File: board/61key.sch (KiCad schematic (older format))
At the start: 134 parts, among them J1 105450-0101, SW1 SW_SPST, SW10 SW_SPST, SW11 SW_SPST, SW12 SW_SPST, SW13 SW_SPST, SW14 SW_SPST, SW15 SW_SPST, SW16 SW_SPST, SW17 SW_SPST, SW18 SW_SPST, SW19 SW_SPST, SW2 SW_SPST, SW20 SW_SPST, SW21 SW_SPST, SW22 SW_SPST, SW23 SW_SPST, SW24 SW_SPST, SW25 SW_SPST, SW26 SW_SPST, SW27 SW_SPST, SW28 SW_SPST, SW29 SW_SPST, SW3 SW_SPST, SW30 SW_SPST, SW31 SW_SPST, SW32 SW_SPST, SW33 SW_SPST, SW34 SW_SPST, SW35 SW_SPST, SW36 SW_SPST, SW37 SW_SPST, SW38 SW_SPST, SW39 SW_SPST, SW4 SW_SPST, SW40 SW_SPST, SW41 SW_SPST, SW42 SW_SPST, SW43 SW_SPST, SW44 SW_SPST, SW45 SW_SPST, SW46 SW_SPST, SW47 SW_SPST, SW48 SW_SPST, SW49 SW_SPST, SW5 SW_SPST, SW50 SW_SPST, SW51 SW_SPST, SW52 SW_SPST, SW53 SW_SPST, SW54 SW_SPST, SW55 SW_SPST, SW56 SW_SPST, SW57 SW_SPST, SW58 SW_SPST, SW59 SW_SPST, SW6 SW_SPST, SW60 SW_SPST, SW61 SW_SPST, SW7 SW_SPST, SW8 SW_SPST, SW9 SW_SPST, U1 ATmega32U4-AU, X1 FA-238

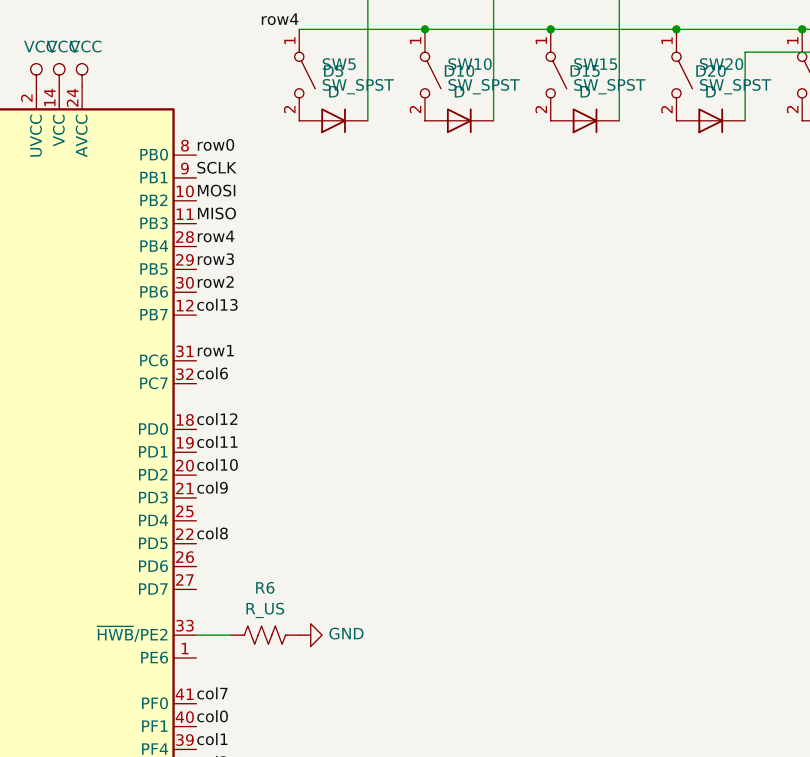
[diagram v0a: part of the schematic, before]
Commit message: add pads, new step
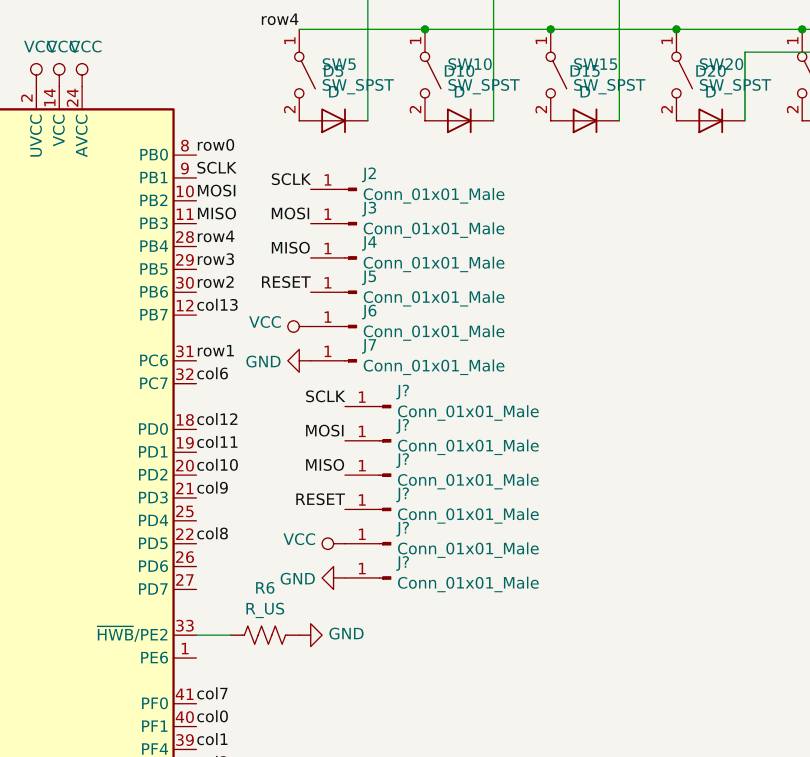
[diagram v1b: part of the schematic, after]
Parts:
- added J2, J3, J4, J5, J6, J7, J? (x6): Conn_01x01_Male, TestPoint:TestPoint_Pad_3.0x3.0mm, symbol Connector:Conn_01x01_Male
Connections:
- net GND: now also J7.1 (Pin_1), J?.1 (Pin_1)
- net MISO: now also J4.1 (Pin_1), J?.1 (Pin_1)
- net MOSI: now also J3.1 (Pin_1), J?.1 (Pin_1)
- net RESET: now also J5.1 (Pin_1), J?.1 (Pin_1)
- net SCLK: now also J2.1 (Pin_1), J?.1 (Pin_1)
- net VCC: now also J6.1 (Pin_1), J?.1 (Pin_1)
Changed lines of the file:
@@
 Text Label 5500 6850 0    50   ~ 0
 col1
+$Comp
+L Connector:Conn_01x01_Male J2
+U 1 1 5EB6BFE2
+P 6200 4400
+F 0 "J2" H 6172 4332 50  0000 R CNN
+F 1 "Conn_01x01_Male" H 6172 4423 50  0000 R CNN
+F 2 "TestPoint:TestPoint_Pad_3.0x3.0mm" H 6200 4400 50  0001 C CNN
+F 3 "~" H 6200 4400 50  0001 C CNN
+	1    6200 4400
+	-1   0    0    1
+$EndComp
+$Comp
+L Connector:Conn_01x01_Male J3
+U 1 1 5EB6DDE5
+P 6200 4550
+F 0 "J3" H 6172 4482 50  0000 R CNN
+F 1 "Conn_01x01_Male" H 6172 4573 50  0000 R CNN
+F 2 "TestPoint:TestPoint_Pad_3.0x3.0mm" H 6200 4550 50  0001 C CNN
+F 3 "~" H 6200 4550 50  0001 C CNN
+	1    6200 4550
+	-1   0    0    1
+$EndComp
+$Comp
+L Connector:Conn_01x01_Male J4
+U 1 1 5EB748FF
+P 6200 4700
+F 0 "J4" H 6172 4632 50  0000 R CNN
+F 1 "Conn_01x01_Male" H 6172 4723 50  0000 R CNN
+F 2 "TestPoint:TestPoint_Pad_3.0x3.0mm" H 6200 4700 50  0001 C CNN
+F 3 "~" H 6200 4700 50  0001 C CNN
+	1    6200 4700
+	-1   0    0    1
+$EndComp
+$Comp
+L Connector:Conn_01x01_Male J5
+U 1 1 5EB7B587
+P 6200 4850
+F 0 "J5" H 6172 4782 50  0000 R CNN
+F 1 "Conn_01x01_Male" H 6172 4873 50  0000 R CNN
+F 2 "TestPoint:TestPoint_Pad_3.0x3.0mm" H 6200 4850 50  0001 C CNN
+F 3 "~" H 6200 4850 50  0001 C CNN
+	1    6200 4850
+	-1   0    0    1
+$EndComp
+Text Label 6000 4400 2    50   ~ 0
+SCLK
+Text Label 6000 4550 2    50   ~ 0
+MOSI
+Text Label 6000 4700 2    50   ~ 0
+MISO
+Text Label 6000 4850 2    50   ~ 0
+RESET
+$Comp
+L Connector:Conn_01x01_Male J6
+U 1 1 5EBD681E
+P 6200 5000
+F 0 "J6" H 6172 4932 50  0000 R CNN
+F 1 "Conn_01x01_Male" H 6172 5023 50  0000 R CNN
+F 2 "TestPoint:TestPoint_Pad_3.0x3.0mm" H 6200 5000 50  0001 C CNN
+F 3 "~" H 6200 5000 50  0001 C CNN
+	1    6200 5000
+	-1   0    0    1
+$EndComp
+$Comp
+L Connector:Conn_01x01_Male J7
+U 1 1 5EBDD458
+P 6200 5150
+F 0 "J7" H 6172 5082 50  0000 R CNN
+F 1 "Conn_01x01_Male" H 6172 5173 50  0000 R CNN
+F 2 "TestPoint:TestPoint_Pad_3.0x3.0mm" H 6200 5150 50  0001 C CNN
+F 3 "~" H 6200 5150 50  0001 C CNN
+	1    6200 5150
+	-1   0    0    1
+$EndComp
+$Comp
+L power:VCC #PWR?
+U 1 1 5EBE65DE
+P 6000 5000
+F 0 "#PWR?" H 6000 4850 50  0001 C CNN
+F 1 "VCC" V 6018 5127 50  0000 L CNN
+F 2 "" H 6000 5000 50  0001 C CNN
+F 3 "" H 6000 5000 50  0001 C CNN
+	1    6000 5000
+	0    -1   -1   0
+$EndComp
+$Comp
+L power:GND #PWR?
+U 1 1 5EBE7004
+P 6000 5150
+F 0 "#PWR?" H 6000 4900 50  0001 C CNN
+F 1 "GND" V 6005 5022 50  0000 R CNN
+F 2 "" H 6000 5150 50  0001 C CNN
+F 3 "" H 6000 5150 50  0001 C CNN
+	1    6000 5150
+	0    1    1    0
+$EndComp
+$Comp
+L Connector:Conn_01x01_Male J?
+U 1 1 5EB751B8
+P 6350 5350
+F 0 "J?" H 6322 5282 50  0000 R CNN
+F 1 "Conn_01x01_Male" H 6322 5373 50  0000 R CNN
+F 2 "TestPoint:TestPoint_Pad_3.0x3.0mm" H 6350 5350 50  0001 C CNN
+F 3 "~" H 6350 5350 50  0001 C CNN
+	1    6350 5350
+	-1   0    0    1
+$EndComp
+$Comp
+L Connector:Conn_01x01_Male J?
+U 1 1 5EB751BE
+P 6350 5500
+F 0 "J?" H 6322 5432 50  0000 R CNN
+F 1 "Conn_01x01_Male" H 6322 5523 50  0000 R CNN
+F 2 "TestPoint:TestPoint_Pad_3.0x3.0mm" H 6350 5500 50  0001 C CNN
+F 3 "~" H 6350 5500 50  0001 C CNN
+	1    6350 5500
+	-1   0    0    1
+$EndComp
+$Comp
+L Connector:Conn_01x01_Male J?
+U 1 1 5EB751C4
+P 6350 5650
+F 0 "J?" H 6322 5582 50  0000 R CNN
+F 1 "Conn_01x01_Male" H 6322 5673 50  0000 R CNN
+F 2 "TestPoint:TestPoint_Pad_3.0x3.0mm" H 6350 5650 50  0001 C CNN
+F 3 "~" H 6350 5650 50  0001 C CNN
+	1    6350 5650
+	-1   0    0    1
+$EndComp
+$Comp
+L Connector:Conn_01x01_Male J?
+U 1 1 5EB751CA
+P 6350 5800
+F 0 "J?" H 6322 5732 50  0000 R CNN
+F 1 "Conn_01x01_Male" H 6322 5823 50  0000 R CNN
+F 2 "TestPoint:TestPoint_Pad_3.0x3.0mm" H 6350 5800 50  0001 C CNN
+F 3 "~" H 6350 5800 50  0001 C CNN
+	1    6350 5800
+	-1   0    0    1
+$EndComp
+Text Label 6150 5350 2    50   ~ 0
+SCLK
+Text Label 6150 5500 2    50   ~ 0
+MOSI
+Text Label 6150 5650 2    50   ~ 0
+MISO
+Text Label 6150 5800 2    50   ~ 0
+RESET
+$Comp
+L Connector:Conn_01x01_Male J?
+U 1 1 5EB751D4
+P 6350 5950
+F 0 "J?" H 6322 5882 50  0000 R CNN
+F 1 "Conn_01x01_Male" H 6322 5973 50  0000 R CNN
+F 2 "TestPoint:TestPoint_Pad_3.0x3.0mm" H 6350 5950 50  0001 C CNN
+F 3 "~" H 6350 5950 50  0001 C CNN
+	1    6350 5950
+	-1   0    0    1
+$EndComp
+$Comp
+L Connector:Conn_01x01_Male J?
+U 1 1 5EB751DA
+P 6350 6100
+F 0 "J?" H 6322 6032 50  0000 R CNN
+F 1 "Conn_01x01_Male" H 6322 6123 50  0000 R CNN
+F 2 "TestPoint:TestPoint_Pad_3.0x3.0mm" H 6350 6100 50  0001 C CNN
+F 3 "~" H 6350 6100 50  0001 C CNN
+	1    6350 6100
+	-1   0    0    1
+$EndComp
+$Comp
+L power:VCC #PWR?
+U 1 1 5EB751E0
+P 6150 5950
+F 0 "#PWR?" H 6150 5800 50  0001 C CNN
+F 1 "VCC" V 6168 6077 50  0000 L CNN
+F 2 "" H 6150 5950 50  0001 C CNN
+F 3 "" H 6150 5950 50  0001 C CNN
+	1    6150 5950
+	0    -1   -1   0
+$EndComp
+$Comp
+L power:GND #PWR?
+U 1 1 5EB751E6
+P 6150 6100
+F 0 "#PWR?" H 6150 5850 50  0001 C CNN
+F 1 "GND" V 6155 5972 50  0000 R CNN
+F 2 "" H 6150 6100 50  0001 C CNN
+F 3 "" H 6150 6100 50  0001 C CNN
+	1    6150 6100
+	0    1    1    0
+$EndComp
 $EndSCHEMATC

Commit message: add board images, remove svg
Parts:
- gave numbers to parts that had none: 6
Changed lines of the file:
@@
 $EndComp
 $Comp
-L Connector:Conn_01x01_Male J?
+L Connector:Conn_01x01_Male J8
 U 1 1 5EB751B8
 P 6350 5350
-F 0 "J?" H 6322 5282 50  0000 R CNN
+F 0 "J8" H 6322 5282 50  0000 R CNN
 F 1 "Conn_01x01_Male" H 6322 5373 50  0000 R CNN
 F 2 "TestPoint:TestPoint_Pad_3.0x3.0mm" H 6350 5350 50  0001 C CNN
@@
 $EndComp
 $Comp
-L Connector:Conn_01x01_Male J?
+L Connector:Conn_01x01_Male J9
 U 1 1 5EB751BE
 P 6350 5500
-F 0 "J?" H 6322 5432 50  0000 R CNN
+F 0 "J9" H 6322 5432 50  0000 R CNN
 F 1 "Conn_01x01_Male" H 6322 5523 50  0000 R CNN
 F 2 "TestPoint:TestPoint_Pad_3.0x3.0mm" H 6350 5500 50  0001 C CNN
@@
 $EndComp
 $Comp
-L Connector:Conn_01x01_Male J?
+L Connector:Conn_01x01_Male J10
 U 1 1 5EB751C4
 P 6350 5650
-F 0 "J?" H 6322 5582 50  0000 R CNN
+F 0 "J10" H 6322 5582 50  0000 R CNN
 F 1 "Conn_01x01_Male" H 6322 5673 50  0000 R CNN
 F 2 "TestPoint:TestPoint_Pad_3.0x3.0mm" H 6350 5650 50  0001 C CNN
@@
 $EndComp
 $Comp
-L Connector:Conn_01x01_Male J?
+L Connector:Conn_01x01_Male J11
 U 1 1 5EB751CA
 P 6350 5800
-F 0 "J?" H 6322 5732 50  0000 R CNN
+F 0 "J11" H 6322 5732 50  0000 R CNN
 F 1 "Conn_01x01_Male" H 6322 5823 50  0000 R CNN
 F 2 "TestPoint:TestPoint_Pad_3.0x3.0mm" H 6350 5800 50  0001 C CNN
@@
 RESET
 $Comp
-L Connector:Conn_01x01_Male J?
+L Connector:Conn_01x01_Male J12
 U 1 1 5EB751D4
 P 6350 5950
-F 0 "J?" H 6322 5882 50  0000 R CNN
+F 0 "J12" H 6322 5882 50  0000 R CNN
 F 1 "Conn_01x01_Male" H 6322 5973 50  0000 R CNN
 F 2 "TestPoint:TestPoint_Pad_3.0x3.0mm" H 6350 5950 50  0001 C CNN
@@
 $EndComp
 $Comp
-L Connector:Conn_01x01_Male J?
+L Connector:Conn_01x01_Male J13
 U 1 1 5EB751DA
 P 6350 6100
-F 0 "J?" H 6322 6032 50  0000 R CNN
+F 0 "J13" H 6322 6032 50  0000 R CNN
 F 1 "Conn_01x01_Male" H 6322 6123 50  0000 R CNN
 F 2 "TestPoint:TestPoint_Pad_3.0x3.0mm" H 6350 6100 50  0001 C CNN

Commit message: new images, backplate, clean up for smt assembly
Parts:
- added C4: C, Capacitor_SMD:C_0805_2012Metric, symbol Device:C
- D1, D10, D11, D12, D13, D14, D15, D16, D17, D18, D19, D2, D20, D21, D22, D23, D24, D25, D26, D27, D28, D29, D3, D30, D31, D32, D33, D34, D35, D36, D37, D38, D39, D4, D40, D41, D42, D43, D44, D45, D46, D47, D48, D49, D5, D50, D51, D52, D53, D54, D55, D56, D57, D58, D59, D6, D60, D61, D7, D8, D9: footprint Diode_SMD:D_0805_2012Metric -> 61key:D_0805_2012Metric
- J10, J11, J12, J13, J2, J3, J4, J5, J6, J7, J8, J9: footprint TestPoint:TestPoint_Pad_3.0x3.0mm -> 61key:pad-nosilk
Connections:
- net GND: now also C4.2
- net RESET: now also C4.1

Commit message: big overhaul
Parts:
- removed C1, C2, C3, C4: C, Capacitor_SMD:C_0805_2012Metric, symbol Device:C
- removed J1: 105450-0101, 61key:MOLEX_105450-0101, symbol 61key:105450-0101
- removed J10, J11, J12, J13, J2, J3, J4, J5, J6, J7, J8, J9: Conn_01x01_Male, 61key:pad-nosilk, symbol Connector:Conn_01x01_Male
- removed R1, R2, R3, R4, R5, R6: R_US, Resistor_SMD:R_0805_2012Metric, symbol Device:R_US
- removed U1: ATmega32U4-AU, 61key:QFN-44-1EP_7x7mm_Pitch0.5mm, symbol MCU_Microchip_ATmega:ATmega32U4-AU
- removed X1: FA-238, 61key:OSCCC320X250X70-4N, symbol 61key:FA-238
- added D62, D63, D64, D65: D, 61key:D_0805_2012Metric, symbol Device:D
- added IC1: STM32F042K6T6, symbol 61key:STM32F042K6T6
- added SW62, SW63, SW64, SW65, SW66, SW67, SW68, SW69, SW70, SW71, SW72, SW73: SW_SPST, 61key:SW_MX, symbol Switch:SW_SPST
- added USB1: 12401598E4#2A, symbol 61key:12401598E4#2A
- SW1, SW11, SW12, SW13, SW14, SW16, SW17, SW18, SW19, SW21, SW22, SW23, SW24, SW26, SW27, SW28, SW29, SW31, SW32, SW33, SW34, SW36, SW37, SW38, SW39, SW41, SW42, SW43, SW44, SW45, SW46, SW47, SW48, SW49, SW50, SW51, SW52, SW53, SW54, SW55, SW57, SW58, SW6, SW7, SW8, SW9: footprint 61key:MX-1U-NoLED -> 61key:SW_MX
- SW10, SW15, SW25, SW30, SW35, SW40, SW5: footprint 61key:MX-1.25U-NoLED -> 61key:SW_MX
- SW2, SW61: footprint 61key:MX-1.5U-NoLED -> 61key:SW_MX
- SW20: footprint 61key:MX-6.25U-NoLED -> 61key:SW_MX
- SW3: footprint 61key:MX-1.75U-NoLED -> 61key:SW_MX
- SW4, SW59: footprint 61key:MX-2.25U-NoLED -> 61key:SW_MX
- SW56: footprint 61key:MX-2.75U-NoLED -> 61key:SW_MX
- SW60: footprint 61key:MX-2U-NoLED -> 61key:SW_MX
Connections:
- net labels added: col14
- net labels removed: GND, MISO, MOSI, RESET, SCLK, VCC
- wire segments 169 -> 138
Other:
- moved on the sheet: D1, D10, D11, D12, D13, D14, D15, D16, D17, D18, D19, D2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

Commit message: layouts done, need to add traces
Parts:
- added SW74, SW75: SW_SPST, 61key:SW_MX, symbol Switch:SW_SPST
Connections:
- wire segments 138 -> 145
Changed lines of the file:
@@
 Connection ~ 10950 2250
 Wire Wire Line
-	10950 2250 11500 2250
+	10950 2250 11400 2250
 $Comp
 L Device:D D2
@@
 	11800 3300 11800 4000
 Wire Wire Line
-	10400 2900 11500 2900
+	10400 2900 11400 2900
 Wire Wire Line
 	7550 4700 7550 4500
@@
 Wire Wire Line
 	10750 4700 10750 4600
-Wire Wire Line
-	11300 4700 11300 4650
 $Comp
 L Device:D D35
@@
 	12000 4700 12100 4700
 Connection ~ 12100 4700
+$Comp
+L Switch:SW_SPST SW74
+U 1 1 5EBE5B89
+P 11400 3100
+F 0 "SW74" V 11354 3198 50  0000 L CNN
+F 1 "SW_SPST" V 11445 3198 50  0000 L CNN
+F 2 "61key:SW_MX" H 11400 3100 50  0001 C CNN
+F 3 "~" H 11400 3100 50  0001 C CNN
+	1    11400 3100
+	0    1    1    0
+$EndComp
+Connection ~ 11400 2900
+Wire Wire Line
+	11400 2900 11500 2900
+Wire Wire Line
+	11400 3300 11500 3300
+Connection ~ 11500 3300
+Wire Wire Line
+	11850 4700 11850 4000
+Wire Wire Line
+	11850 4000 11800 4000
+Connection ~ 11800 4000
+Wire Wire Line
+	11300 4000 10700 4000
+Wire Wire Line
+	11300 4000 11300 4700
+Connection ~ 10700 4000
+$Comp
+L Switch:SW_SPST SW75
+U 1 1 5EC4B4E8
+P 11400 2450
+F 0 "SW75" V 11354 2548 50  0000 L CNN
+F 1 "SW_SPST" V 11445 2548 50  0000 L CNN
+F 2 "61key:SW_MX" H 11400 2450 50  0001 C CNN
+F 3 "~" H 11400 2450 50  0001 C CNN
+	1    11400 2450
+	0    1    1    0
+$EndComp
+Connection ~ 11400 2250
+Wire Wire Line
+	11400 2250 11500 2250
+Wire Wire Line
+	11400 2650 11500 2650
+Connection ~ 11500 2650
 $EndSCHEMATC

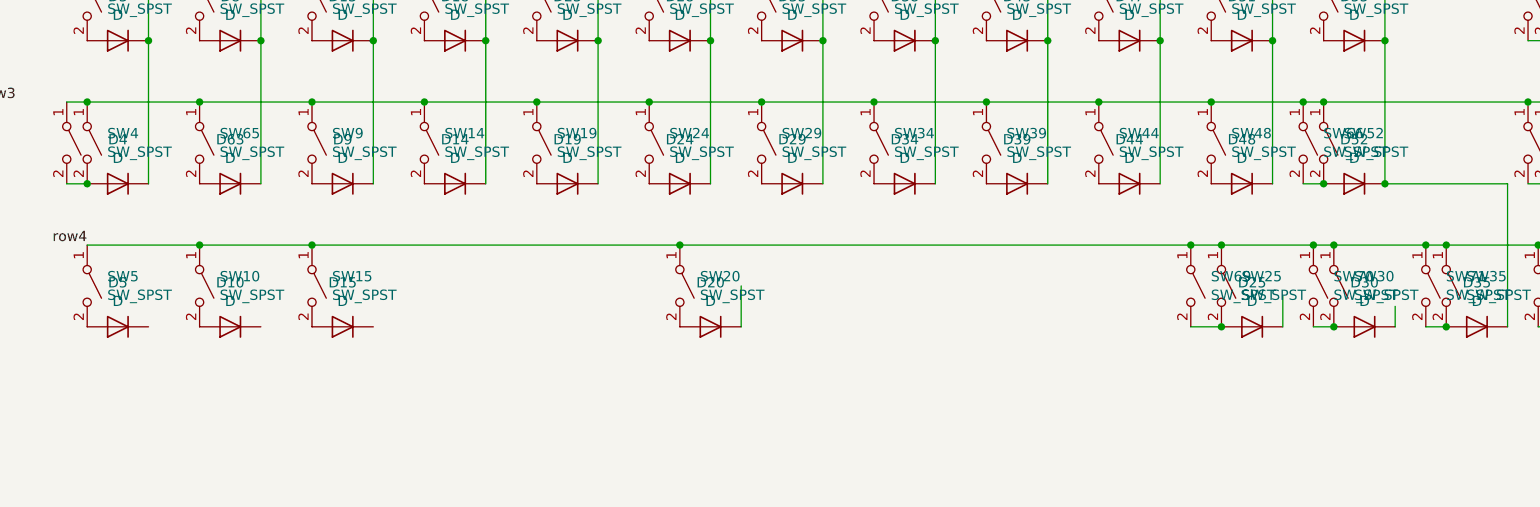
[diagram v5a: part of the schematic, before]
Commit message: rows and columns for all layouts done
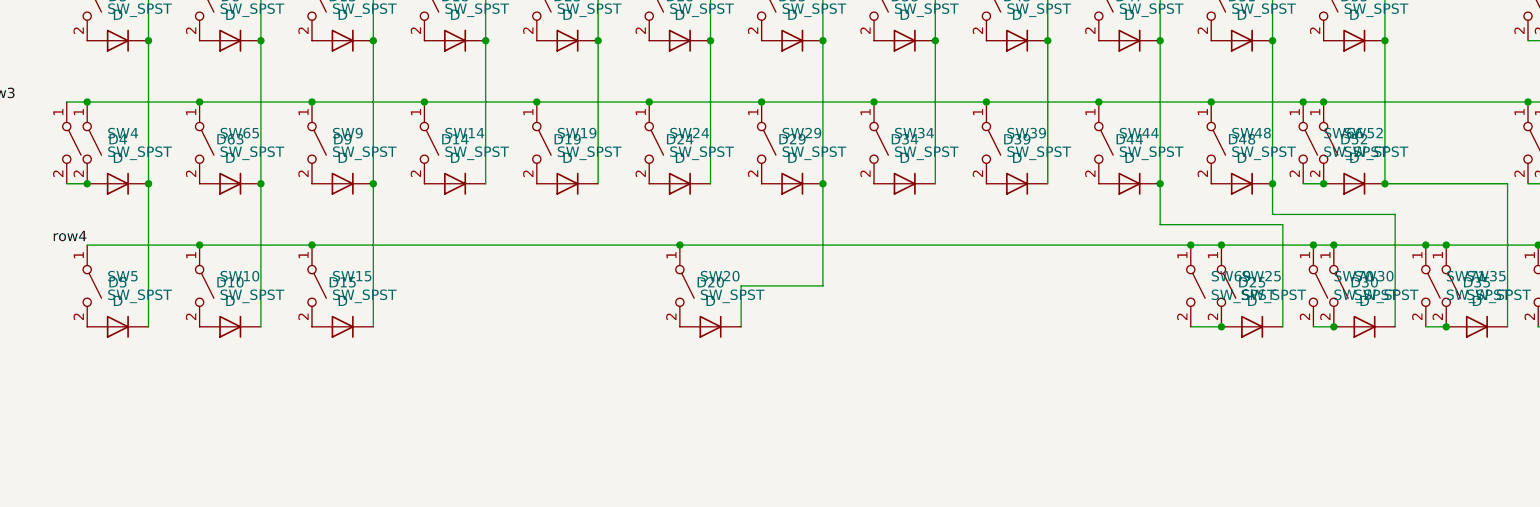
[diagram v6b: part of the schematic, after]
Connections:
- net col0: now also D5.1 (K)
- net col1: now also D10.1 (K)
- net col10: now also D30.1 (K)
- net col2: now also D15.1 (K)
- net col6: now also D20.1 (K)
- net col9: now also D25.1 (K)
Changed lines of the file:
@@
 Wire Wire Line
 	7550 4700 7550 4500
-Wire Wire Line
-	10200 4700 10200 4550
-Wire Wire Line
-	10750 4700 10750 4600
 $Comp
 L Device:D D35
@@
 	11400 2650 11500 2650
 Connection ~ 11500 2650
+Wire Wire Line
+	5200 4700 5200 4000
+Connection ~ 5200 4000
+Wire Wire Line
+	5750 4700 5750 4000
+Connection ~ 5750 4000
+Wire Wire Line
+	4650 4700 4650 4000
+Connection ~ 4650 4000
+Wire Wire Line
+	7550 4500 7950 4500
+Wire Wire Line
+	7950 4500 7950 4000
+Connection ~ 7950 4000
+Wire Wire Line
+	10750 4150 10150 4150
+Wire Wire Line
+	10150 4150 10150 4000
+Wire Wire Line
+	10750 4150 10750 4700
+Connection ~ 10150 4000
+Wire Wire Line
+	10200 4200 9600 4200
+Wire Wire Line
+	9600 4200 9600 4000
+Wire Wire Line
+	10200 4200 10200 4700
+Connection ~ 9600 4000
 $EndSCHEMATC
